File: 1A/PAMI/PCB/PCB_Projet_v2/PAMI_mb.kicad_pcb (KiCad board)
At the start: 4 copper layers, 66.5 x 58.4 mm, 107 parts, among them J1 Conn_02x20_Odd_Even, J10 Conn_01x04, J11 Conn_01x04, J12 Conn_01x04, J13 Conn_01x04, J2 Conn_01x03, J3 Conn_ST_STDC14, J4 Battery, J5 Charge, J6 Stop, J8 173010542, J9 Conn_01x04, SW1 SW_Push_SPDT, SW2 RotaryEncoder_Switch, SW3 SW_Push, SW4 SW_Push, SW5 SW_Push, SW6 SW_Push, U1 STM32G431KBTx, U2 LT1076CR-PBF, U3 AZ1117CH2-3.3TRG1, U4 TMC2225-SA-T, U5 TMC2225-SA-T

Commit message: update pcb
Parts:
- C16, C17, C18: footprint Capacitor_THT:CP_Radial_Tantal_D6.0mm_P2.50mm -> Capacitor_SMD:CP_Elec_6.3x5.4
- C19, C20, C21, C22, C23, C24, C25, C26, C27: footprint Capacitor_SMD:C_0603_1608Metric -> Capacitor_SMD:C_0402_1005Metric
- J3: footprint Connector_PinSocket_2.54mm:PinSocket_2x07_P2.54mm_Vertical -> Connector_PinHeader_1.27mm:PinHeader_2x07_P1.27mm_Vertical_SMD
- L1: footprint Inductor_SMD:L_0201_0603Metric -> Inductor_SMD:L_Changjiang_FNR8065S
- R25, R26, R32, R33: footprint Resistor_SMD:R_0402_1005Metric -> Resistor_SMD:R_1206_3216Metric
- SW1: footprint MINI_SPDT_SW:SW_MINI-SPDT-SW -> Library:472121010111
- SW3, SW4, SW5, SW6: footprint Button_Switch_THT:SW_PUSH_6mm -> Button_Switch_SMD:SW_Push_1P1T_NO_6x6mm_H9.5mm
- U3: footprint AZ1117_CH2:SOT230P700X180-4N -> Package_TO_SOT_SMD:SOT-223-3_TabPin2
- moved U3 112.0 mm to (37.5, 85.5)
- moved C25 112.0 mm to (74.9, 59.8), turned to -90 degrees
- moved R35 109.0 mm to (74.8, 55.8), turned to -90 degrees
- moved R36 105.6 mm to (74.9, 57.8), turned to -90 degrees
- moved C1 99.9 mm to (53.0, 103.5)
- moved C13 99.9 mm to (51.8, 103.6)
- moved C2 99.9 mm to (54.4, 103.5)
- moved C26 99.9 mm to (86.9, 74.2)
- moved C3 99.9 mm to (56.4, 103.5)
- moved R11 99.9 mm to (71.1, 92.6)
- moved R39 99.9 mm to (84.0, 84.3)
- moved R40 99.9 mm to (80.8, 84.2)
- moved C10 99.9 mm to (71.1, 96.8)
- moved C12 99.9 mm to (39.3, 64.0)
- moved C17 99.9 mm to (56.2, 85.1)
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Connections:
- J11 pad 1: /TMC2225/OA1 -> /TMC2225/OA2
- J11 pad 2: /TMC2225/OA2 -> /TMC2225/OA1
- J12 pad 1: /TMC2226/OA1 -> /TMC2226/OA2
- J12 pad 2: /TMC2226/OA2 -> /TMC2226/OA1
- J4 pad 1: GND -> /V_BAT
- J4 pad 2: /V_BAT -> GND
- J5 pad 1: GND -> /V_CHARGE
- J5 pad 2: /V_CHARGE -> GND
- J6 pad 1: Net-(J6-Pin_1) -> VCC
- J6 pad 2: VCC -> Net-(J6-Pin_2)
- SW1 pad 1: Net-(J6-Pin_1) -> Net-(J6-Pin_2)
- U1 pad 10: /PWM_MOTOR_L_TIM2_CH1 -> /PWM_MOTOR_R_TIM3_CH1
- U1 pad 11: /PWM_MOTOR_R_TIM3_CH1 -> /PWM_MOTOR_L_TIM2_CH1
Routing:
- net +3.3V: track 195.6 -> 0.00 mm, vias 14 -> 0
- net GND: track 180.6 -> 0.00 mm, vias 21 -> 0
- net VCC: track 115.3 -> 0.00 mm, vias 5 -> 0
- net /PA1_USR_BTN_0: track 79.0 -> 3.53 mm, vias 4 -> 0
- net /LIDAR_LP_TX: track 69.6 -> 0.00 mm, vias 2 -> 0
- net /ENCODEUR_B: track 62.4 -> 0.00 mm, vias 2 -> 0
- net /RASPBERRY_PI_RX: track 61.0 -> 0.00 mm, vias 10 -> 0
- net /PA11_USR_BTN_1: track 59.9 -> 0.00 mm, vias 8 -> 0
- net /PB8-BOOT0_LED0: track 55.5 -> 0.00 mm, vias 6 -> 0
- net /DIR_MOTOR_L: track 53.4 -> 0.00 mm, vias 4 -> 0
- net /NRST: track 52.4 -> 0.00 mm, vias 3 -> 0
- net /RASPBERRY_PI_TX: track 52.2 -> 0.00 mm, vias 2 -> 0
- net /ADC_BATT: track 52.0 -> 0.00 mm, vias 6 -> 0
- net /SWCLK: track 46.5 -> 0.00 mm, vias 3 -> 0
- net /PA12_USR_BTN_2: track 45.2 -> 0.00 mm, vias 2 -> 0
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- removed copper zone on In1.Cu, net +3.3V
- removed copper zone on In1.Cu, net +5.1V
- removed copper zone on In1.Cu, net +5V
- removed copper zone on In1.Cu, net /V_BAT
- removed copper zone on In1.Cu, net /V_CHARGE
- removed copper zone on In1.Cu, net VCC
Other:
- board size 66.5 x 58.4 mm -> 65 x 56 mm

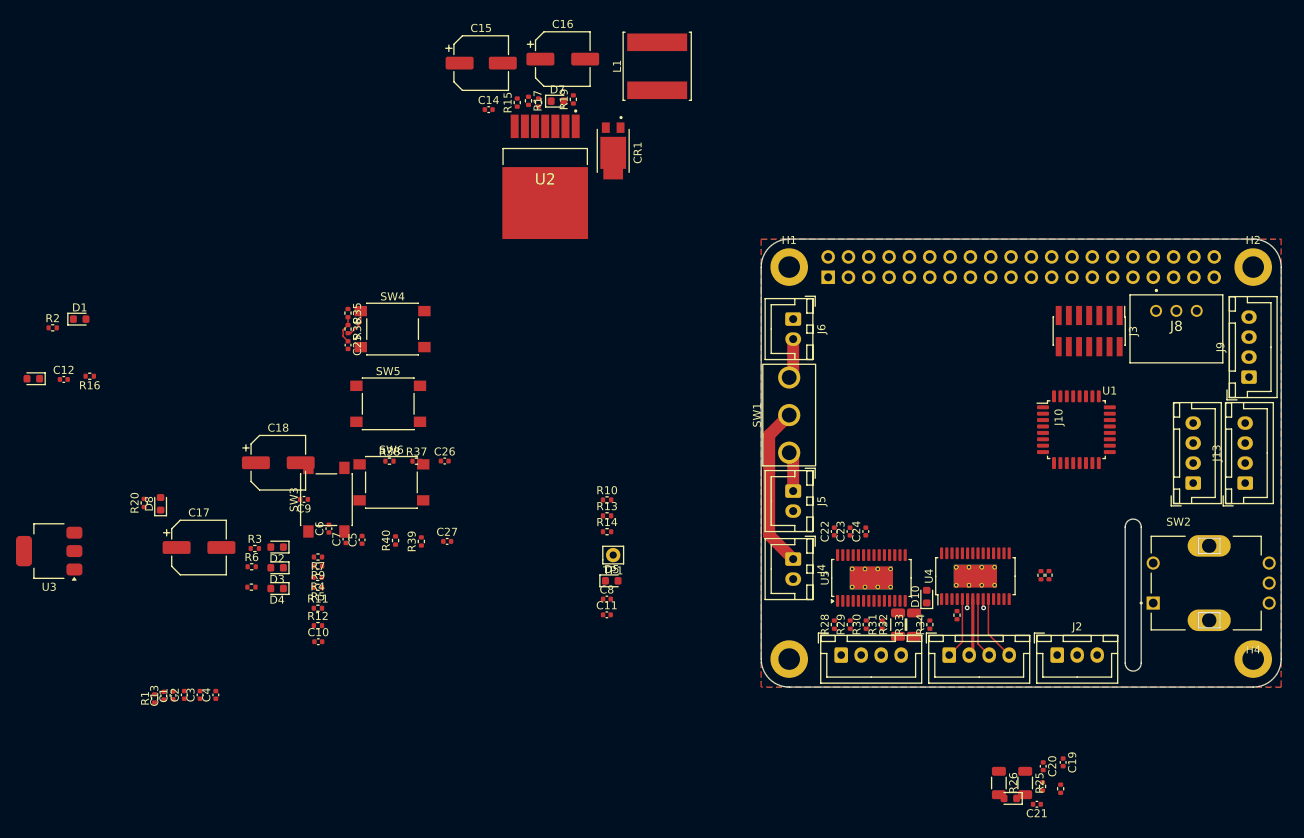
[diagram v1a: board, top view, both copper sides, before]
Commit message: update PCB placement
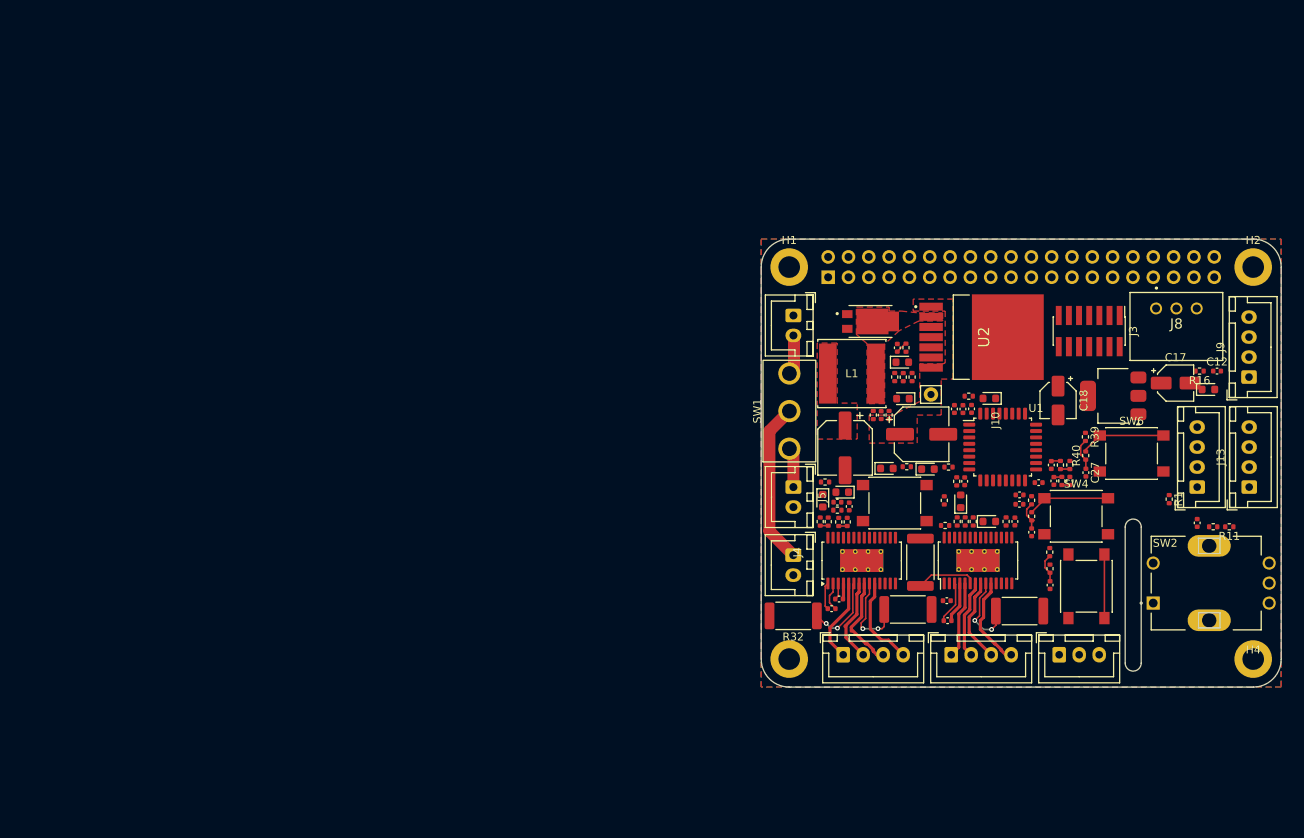
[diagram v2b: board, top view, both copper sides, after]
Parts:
- C17, C18: footprint Capacitor_SMD:CP_Elec_6.3x5.4 -> Capacitor_SMD:CP_Elec_4x5.4
- R25, R26, R32, R33: footprint Resistor_SMD:R_1206_3216Metric -> Resistor_SMD:R_2512_6332Metric
- moved D6 146.9 mm to (182.4, 65.3), turned to 0 degrees
- moved C12 144.2 mm to (183.5, 63.0)
- moved R16 138.7 mm to (181.3, 63.0)
- moved U3 134.4 mm to (170.5, 66.1)
- moved R1 129.2 mm to (177.5, 79.0), turned to -90 degrees
- moved C17 123.8 mm to (178.3, 64.5)
- moved R11 114.4 mm to (185.0, 82.5), turned to 180 degrees
- moved R12 112.6 mm to (183.0, 82.5), turned to 180 degrees
- moved C10 110.9 mm to (181.0, 82.0), turned to 90 degrees
- moved C3 105.2 mm to (158.8, 79.7), turned to 180 degrees
- moved C13 105.1 mm to (150.7, 67.7)
- moved C1 105.0 mm to (151.7, 67.7)
- moved C2 104.7 mm to (152.8, 67.7)
- moved C4 103.5 mm to (158.8, 78.5), turned to 180 degrees
- moved R20 100.0 mm to (149.4, 79.2)
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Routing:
- net /TMC2226/OB1: track 0.00 -> 11.9 mm
- net /TMC2226/OB2: track 0.00 -> 11.4 mm
- net Net-(U5-BRB): track 0.00 -> 11.1 mm, vias 0 -> 2
- net Net-(R40-Pad2): track 0.00 -> 10.7 mm
- net /TMC2226/OA1: track 0.00 -> 10.6 mm
- net /TMC2226/OA2: track 0.00 -> 10.6 mm
- net Net-(U5-BRA): track 0.00 -> 9.63 mm, vias 0 -> 2
- net Net-(U4-BRB): track 1.12 -> 10.3 mm, vias 1 -> 2
- net Net-(R38-Pad2): track 0.00 -> 8.00 mm
- net VCC: track 0.00 -> 7.13 mm
- net Net-(R36-Pad2): track 3.61 -> 10.4 mm
- net Net-(U4-BRA): track 1.12 -> 7.60 mm, vias 1 -> 0
- net Net-(U4-VCP): track 0.00 -> 5.33 mm
- net /PA12_USR_BTN_2: track 0.00 -> 3.98 mm
- net Net-(U5-CPI): track 0.00 -> 3.64 mm
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- added copper zone on F.Cu, net +5.1V
- added copper zone on F.Cu, net /Vsw
- added copper zone on F.Cu, net VCC

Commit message: update PAMI pcb
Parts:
- removed C10, C6: 10n, Capacitor_SMD:C_0402_1005Metric
- removed C17, C18: 10u, Capacitor_SMD:CP_Elec_4x5.4
- removed C19, C22: 100nF, Capacitor_SMD:C_0402_1005Metric
- removed C20, C23: 22nF, Capacitor_SMD:C_0402_1005Metric
- removed C21, C24: 2.2uF, Capacitor_SMD:C_0402_1005Metric
- removed C8: 10u, Capacitor_SMD:C_0402_1005Metric
- removed D10, D9: LED, LED_SMD:LED_0603_1608Metric
- removed J10: Conn_01x04, Connector_JST:JST_XH_B4B-XH-A_1x04_P2.50mm_Vertical
- removed R21, R22, R23, R24, R28, R29, R30, R31: 0R, Resistor_SMD:R_0402_1005Metric
- removed R25, R26, R32, R33: 150m, Resistor_SMD:R_2512_6332Metric
- removed R27, R34: 1k, Resistor_SMD:R_0402_1005Metric
- removed U4, U5: TMC2225-SA-T, Package_SO:HTSSOP-28-1EP_4.4x9.7mm_P0.65mm_EP2.85x5.4mm_ThermalVias
- added C106: 10n, Capacitor_SMD:C_0402_1005Metric, F.Cu at (190.0, 95.4)
- added C110: 10n, Capacitor_SMD:C_0402_1005Metric, F.Cu at (175.3, 95.4)
- added C117: 10u, Capacitor_SMD:C_0603_1608Metric, F.Cu at (163.6, 61.3)
- added C118: 10u, Capacitor_SMD:C_0603_1608Metric, F.Cu at (163.6, 65.5)
- added C201: 100nF, Capacitor_SMD:C_0402_1005Metric, F.Cu at (159.1, 95.3)
- added C202: 22nF, Capacitor_SMD:C_0402_1005Metric, F.Cu at (157.2, 95.3)
- added C203: 2.2uF, Capacitor_SMD:C_0402_1005Metric, F.Cu at (166.5, 86.5)
- added C301: 100nF, Capacitor_SMD:C_0402_1005Metric, F.Cu at (140.5, 95.3)
- added C302: 22nF, Capacitor_SMD:C_0402_1005Metric, F.Cu at (138.6, 95.3)
- added C303: 2.2uF, Capacitor_SMD:C_0402_1005Metric, F.Cu at (147.9, 86.5)
- added D201: LED, LED_SMD:LED_0603_1608Metric, F.Cu at (164.8, 85.5)
- added D301: LED, LED_SMD:LED_0603_1608Metric, F.Cu at (146.2, 85.5)
- added J110: Conn_01x04, Connector_JST:JST_XH_B4B-XH-A_1x04_P2.50mm_Vertical, F.Cu at (187.5, 76.8)
- added R201: 0R, Resistor_SMD:R_0402_1005Metric, F.Cu at (160.1, 86.5)
- added R202: 0R, Resistor_SMD:R_0402_1005Metric, F.Cu at (160.1, 85.5)
- added R203: 0R, Resistor_SMD:R_0402_1005Metric, F.Cu at (158.2, 86.5)
- added R204: 0R, Resistor_SMD:R_0402_1005Metric, F.Cu at (158.2, 85.5)
- added R205: 150m, Resistor_SMD:R_2512_6332Metric, F.Cu at (154.8, 90.9)
- added R206: 150m, Resistor_SMD:R_2512_6332Metric, F.Cu at (168.9, 90.9)
- added R207: 1k, Resistor_SMD:R_0402_1005Metric, F.Cu at (163.6, 86.1)
- added R301: 0R, Resistor_SMD:R_0402_1005Metric, F.Cu at (141.5, 86.5)
- added R302: 0R, Resistor_SMD:R_0402_1005Metric, F.Cu at (141.5, 85.5)
- added R303: 0R, Resistor_SMD:R_0402_1005Metric, F.Cu at (139.6, 86.5)
- added R304: 0R, Resistor_SMD:R_0402_1005Metric, F.Cu at (139.6, 85.5)
- added R305: 150m, Resistor_SMD:R_2512_6332Metric, F.Cu at (136.2, 90.9)
- added R306: 150m, Resistor_SMD:R_2512_6332Metric, F.Cu at (150.3, 90.9)
- added R307: 1k, Resistor_SMD:R_0402_1005Metric, F.Cu at (145.0, 86.1)
- added U201: TMC2225-SA-T, Package_SO:HTSSOP-28-1EP_4.4x9.7mm_P0.65mm_EP2.85x5.4mm_ThermalVias, F.Cu at (161.8, 90.9)
- added U301: TMC2225-SA-T, Package_SO:HTSSOP-28-1EP_4.4x9.7mm_P0.65mm_EP2.85x5.4mm_ThermalVias, F.Cu at (143.2, 90.9)
- L101: renamed from L1; footprint Inductor_SMD:L_Changjiang_FNR8065S -> Inductor_SMD:L_Wuerth_WE-PD2-Typ-L
- moved C113 41.4 mm to (190.1, 80.3), turned to 0 degrees
- moved D106 39.3 mm to (146.3, 80.9), turned to 90 degrees
- moved R116 38.2 mm to (146.3, 78.4), turned to -90 degrees
- moved R105 30.5 mm to (188.2, 95.4), turned to 0 degrees
- moved C109 28.6 mm to (153.7, 56.4), turned to 90 degrees
- moved R109 28.3 mm to (186.3, 95.4), turned to 180 degrees
- moved C105 28.2 mm to (190.1, 81.8), turned to 0 degrees
- moved SW103 28.1 mm to (159.2, 56.4), turned to 180 degrees
- moved C501 28.0 mm to (176.8, 65.6), turned to 180 degrees
- moved SW501 25.6 mm to (170.9, 64.6), turned to 180 degrees
- moved R502 25.5 mm to (176.8, 66.5), turned to 180 degrees
- moved R103 25.3 mm to (188.2, 81.8), turned to 180 degrees
- moved C107 23.3 mm to (184.0, 81.8)
- moved R501 23.1 mm to (176.8, 67.5), turned to 0 degrees
- moved R101 23.0 mm to (157.3, 68.0), turned to 90 degrees
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- renumbered C1 to C101, C2 to C102, C3 to C103, C4 to C104, C5 to C105, C7 to C107, C9 to C109, C11 to C111, C12 to C112, C13 to C113, C14 to C114, C15 to C115, C16 to C116, C25 to C401, C26 to C501, C27 to C601, CR1 to CR101, D1 to D101, D2 to D102, D3 to D103, D4 to D104, D5 to D105, D6 to D106, D7 to D107, D8 to D108, H1 to H101, H2 to H102, H3 to H103, H4 to H104, J1 to J101, J2 to J102, J3 to J103, J4 to J104, J5 to J105, J6 to J106, J13 to J107, J8 to J108, J9 to J109, J11 to J111, J12 to J112, R1 to R101, R2 to R102, R5 to R103, R3 to R104, R4 to R105, R6 to R106, R7 to R107, R8 to R108, R9 to R109, R10 to R110, R11 to R111, R13 to R112, R14 to R113, R12 to R114, R15 to R115, R16 to R116, R17 to R117, R18 to R118, R19 to R119, R20 to R120, R35 to R401, R36 to R402, R37 to R501, R38 to R502, R39 to R601, R40 to R602, SW1 to SW101, SW2 to SW102, SW3 to SW103, SW4 to SW401, SW5 to SW501, SW6 to SW601, TP1 to TP101, U1 to U101, U2 to U102, U3 to U103
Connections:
- C105 pad 1: /ENCODEUR_B -> Net-(C105-Pad1)
- R103 pad 2: Net-(R5-Pad2) -> Net-(C105-Pad1)
- R107 pad 1: Net-(R5-Pad2) -> Net-(C105-Pad1)
- R111 pad 2: Net-(R11-Pad2) -> Net-(C110-Pad1)
- R114 pad 1: Net-(R11-Pad2) -> Net-(C110-Pad1)
- SW102 pad B: Net-(R5-Pad2) -> Net-(C105-Pad1)
- SW102 pad S1: Net-(R11-Pad2) -> GND
- SW102 pad S2: GND -> Net-(C110-Pad1)
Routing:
- net GND: track 0.00 -> 68.4 mm, vias 0 -> 57
- net VCC: track 7.13 -> 70.9 mm, vias 0 -> 21
- net +5V: track 0.00 -> 41.3 mm, vias 0 -> 1
- net +3.3V: track 0.00 -> 33.4 mm, vias 0 -> 23
- net /SWDIO: track 0.00 -> 21.4 mm
- net /SWCLK: track 0.00 -> 19.5 mm
- net /STLINK_RX: track 0.00 -> 19.2 mm
- net /NRST: track 0.00 -> 17.7 mm, vias 0 -> 2
- net /STLINK_TX: track 0.00 -> 14.9 mm
- net /V_CHARGE: track 5.01 -> 16.4 mm
- net Net-(U5-BRB): track 11.1 -> 0.00 mm, vias 2 -> 0
- net Net-(U4-BRB): track 10.3 -> 0.00 mm, vias 2 -> 0
- net /VFB: track 0.00 -> 9.69 mm, vias 0 -> 2
- net Net-(U5-BRA): track 9.63 -> 0.00 mm, vias 2 -> 0
- net Net-(U4-BRA): track 7.60 -> 0.00 mm
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- added copper zone on F.Cu, net +3.3V
- added copper zone on In1.Cu, net +3.3V
- added copper zone on In1.Cu, net +5.1V
- added copper zone on B.Cu, net Net-(U301-BRA)
- added copper zone on F.Cu, net Net-(U301-BRA)
- added copper zone on B.Cu, net Net-(U301-BRB)
- added copper zone on F.Cu, net Net-(U301-BRB)
- added copper zone on In1.Cu, net VCC

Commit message: update pcb PAMI
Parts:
- moved C111 3.24 mm to (151.2, 72.6)
- moved R112 3.24 mm to (151.2, 70.6)
- moved R113 3.24 mm to (151.2, 71.6)
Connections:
- U101 pad 12: /DIR_MOTOR_R -> /DIR_MOTOR_L
- U101 pad 20: /RASPBERRY_PI_RX -> /LIDAR_LP_RX
- U101 pad 22: /PA12_USR_BTN_2 -> /PA1_USR_BTN_0
- U101 pad 29: /RASPBERRY_PI_TX -> /LIDAR_LP_TX
- U101 pad 6: /PA1_USR_BTN_0 -> /PA12_USR_BTN_2
- U101 pad 7: /LIDAR_LP_TX -> /RASPBERRY_PI_TX
- U101 pad 8: /LIDAR_LP_RX -> /RASPBERRY_PI_RX
- U101 pad 9: /DIR_MOTOR_L -> /DIR_MOTOR_R
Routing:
- net /PA11_USR_BTN_1: track 1.92 -> 21.5 mm
- net /PWM_MOTOR_R_TIM3_CH1: track 3.55 -> 21.3 mm
- net /PA1_USR_BTN_0: track 1.86 -> 17.0 mm
- net /PB8-BOOT0_LED0: track 1.53 -> 15.7 mm
- net /PF0_LED1: track 0.00 -> 7.92 mm
- net /PWM_MOTOR_L_TIM2_CH1: track 3.55 -> 11.2 mm
- net /DIR_MOTOR_L: track 3.61 -> 11.2 mm
- net /PF1_LED2: track 0.00 -> 6.64 mm
- net VCC: track 70.9 -> 75.1 mm, vias 21 -> 29
- net /ADC_BATT: track 4.20 -> 6.80 mm, vias 0 -> 2
- added copper zone on B.Cu, net Net-(U201-BRA)
- added copper zone on B.Cu, net Net-(U201-BRB)

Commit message: update pcb new
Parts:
- moved J110 0.75 mm to (187.8, 77.5)
- moved C113 0.60 mm to (190.1, 80.9)
- moved J109 0.46 mm to (187.8, 64.0)
- moved C112 0.30 mm to (186.0, 53.0)
- moved C202 0.23 mm to (157.0, 95.3)
- moved C302 0.16 mm to (138.4, 95.3)
- moved C301 0.08 mm to (140.4, 95.3)
- moved C401 0.08 mm to (176.9, 70.4)
- moved C201 0.08 mm to (159.0, 95.3)
- moved C106 0.07 mm to (190.1, 95.4)
- moved C105 0.07 mm to (190.2, 81.8)
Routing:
- net /DATA_RECEIVER: track 0.00 -> 46.3 mm, vias 0 -> 2
- net /RASPBERRY_PI_RX: track 0.00 -> 42.3 mm, vias 0 -> 2
- net /LIDAR_LP_RX: track 0.00 -> 41.7 mm
- net /RASPBERRY_PI_TX: track 0.00 -> 39.2 mm, vias 0 -> 2
- net /ENCODEUR_A: track 0.00 -> 34.8 mm
- net /LIDAR_LP_TX: track 0.00 -> 33.9 mm, vias 0 -> 2
- net /I2C_SDA: track 0.00 -> 32.4 mm, vias 0 -> 1
- net /ENCODEUR_BTN: track 0.00 -> 31.8 mm
- net /I2C_SCL: track 0.00 -> 28.8 mm, vias 0 -> 4
- net /ENCODEUR_B: track 0.00 -> 27.9 mm
- net /PB8-BOOT0_LED0: track 15.7 -> 43.4 mm, vias 0 -> 1
- net /PF1_LED2: track 6.64 -> 34.2 mm, vias 0 -> 2
- net /PF0_LED1: track 7.92 -> 34.9 mm, vias 0 -> 2
- net +5V: track 41.3 -> 68.0 mm, vias 1 -> 3
- net /PA12_USR_BTN_2: track 1.96 -> 25.8 mm, vias 0 -> 2
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
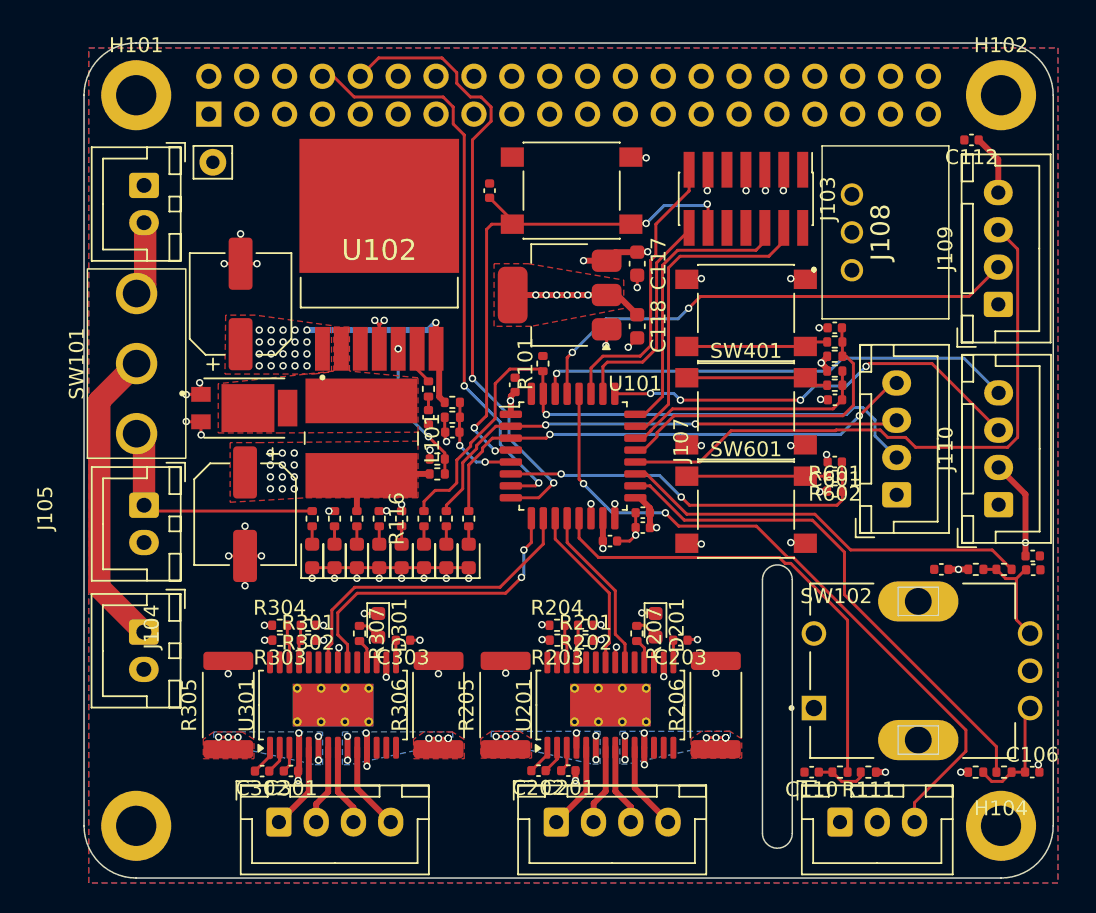
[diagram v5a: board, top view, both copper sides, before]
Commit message: pcb PAMI fix bugs
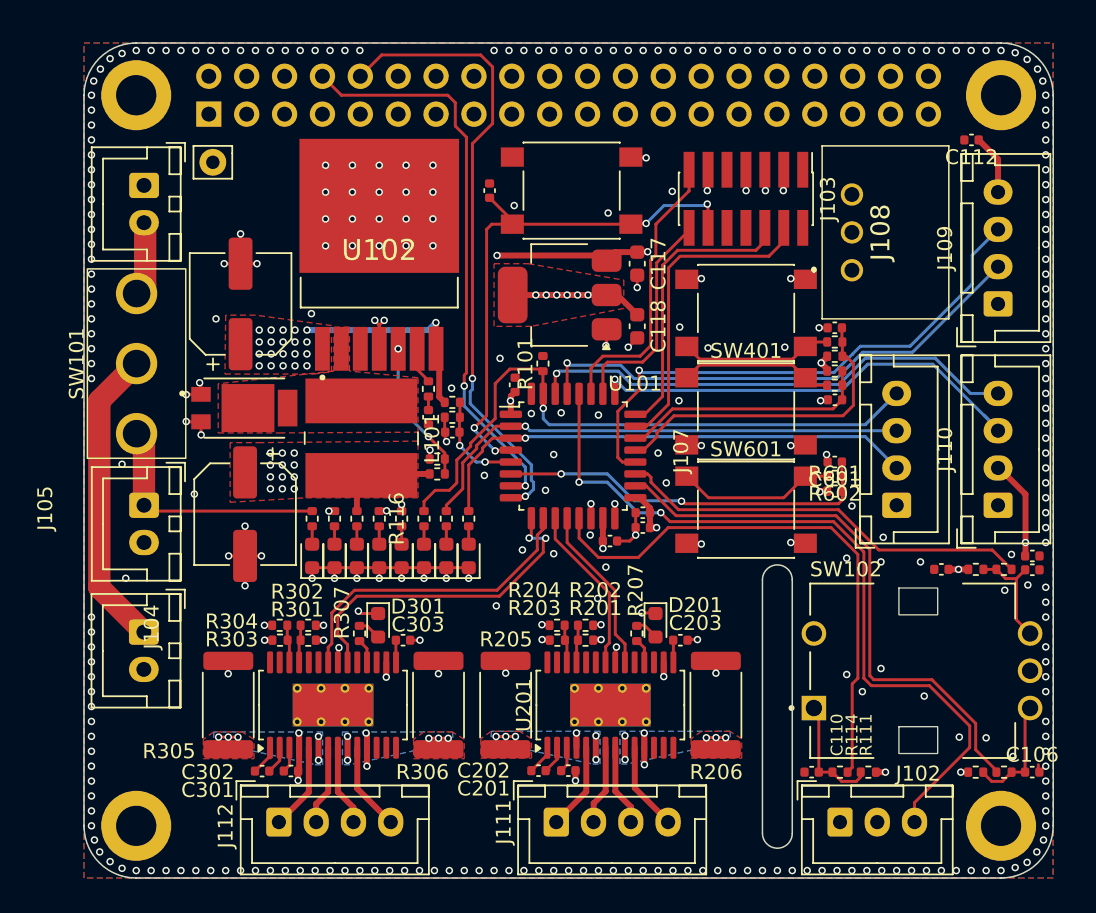
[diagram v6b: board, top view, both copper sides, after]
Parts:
- moved J107 0.70 mm to (181.0, 77.5)
- moved C105 0.06 mm to (190.1, 81.8)
- moved J110 0.05 mm to (187.8, 77.5)
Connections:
- J107 pad 2: /PB8-BOOT0_LED0 -> /PF1_LED2
- J107 pad 4: /PF1_LED2 -> /PB8-BOOT0_LED0
- SW102 pad S1: GND -> Net-(C110-Pad1)
- SW102 pad S2: Net-(C110-Pad1) -> GND
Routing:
- net /DATA_RECEIVER: track 46.3 -> 51.9 mm
- net /ENCODEUR_BTN: track 31.8 -> 37.0 mm
- net /LIDAR_LP_RX: track 41.7 -> 37.0 mm, vias 0 -> 1
- net Net-(C110-Pad1): track 3.57 -> 8.00 mm
- net /ENCODEUR_A: track 34.8 -> 38.2 mm
- net /I2C_SCL: track 28.8 -> 31.0 mm, vias 4 -> 1
- net +5V: track 68.0 -> 69.6 mm
- net /DIR_MOTOR_R: track 21.1 -> 22.5 mm
- net Net-(R602-Pad2): track 9.42 -> 10.6 mm
- net /PF0_LED1: track 34.9 -> 34.1 mm, vias 2 -> 1
- net /RASPBERRY_PI_TX: track 39.2 -> 38.4 mm
- net /PB8-BOOT0_LED0: track 43.4 -> 42.7 mm
- net /I2C_SDA: track 32.4 -> 33.2 mm
- net Net-(R402-Pad2): track 9.62 -> 10.3 mm
- net Net-(R502-Pad2): track 9.54 -> 10.2 mm
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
